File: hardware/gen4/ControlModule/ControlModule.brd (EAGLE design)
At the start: 29.9 x 59.3 mm, 39 parts, among them IC1 XMEGA16A4A

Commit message: changed a resistor value
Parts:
- R8: value 80k -> 80.6k
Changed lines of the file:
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@@
 <?xml version="1.0" encoding="utf-8"?>
 <!DOCTYPE eagle SYSTEM "eagle.dtd">
-<eagle version="7.2.0">
+<eagle version="7.5.0">
 <drawing>
 <settings>
@@
 <attribute name="VALUE" x="41.024" y="8.522" size="0.4064" layer="28" rot="MR180"/>
 </element>
-<element name="R8" library="SparkFun-Passives" package="0805" value="80k" x="44.45" y="20.0025" smashed="yes" rot="MR0">
+<element name="R8" library="SparkFun-Passives" package="0805" value="80.6k" x="44.45" y="20.0025" smashed="yes" rot="MR0">
 <attribute name="NAME" x="45.412" y="21.128" size="0.4064" layer="26" rot="MR0"/>
 <attribute name="VALUE" x="44.166" y="21.2055" size="0.4064" layer="28" rot="MR0"/>

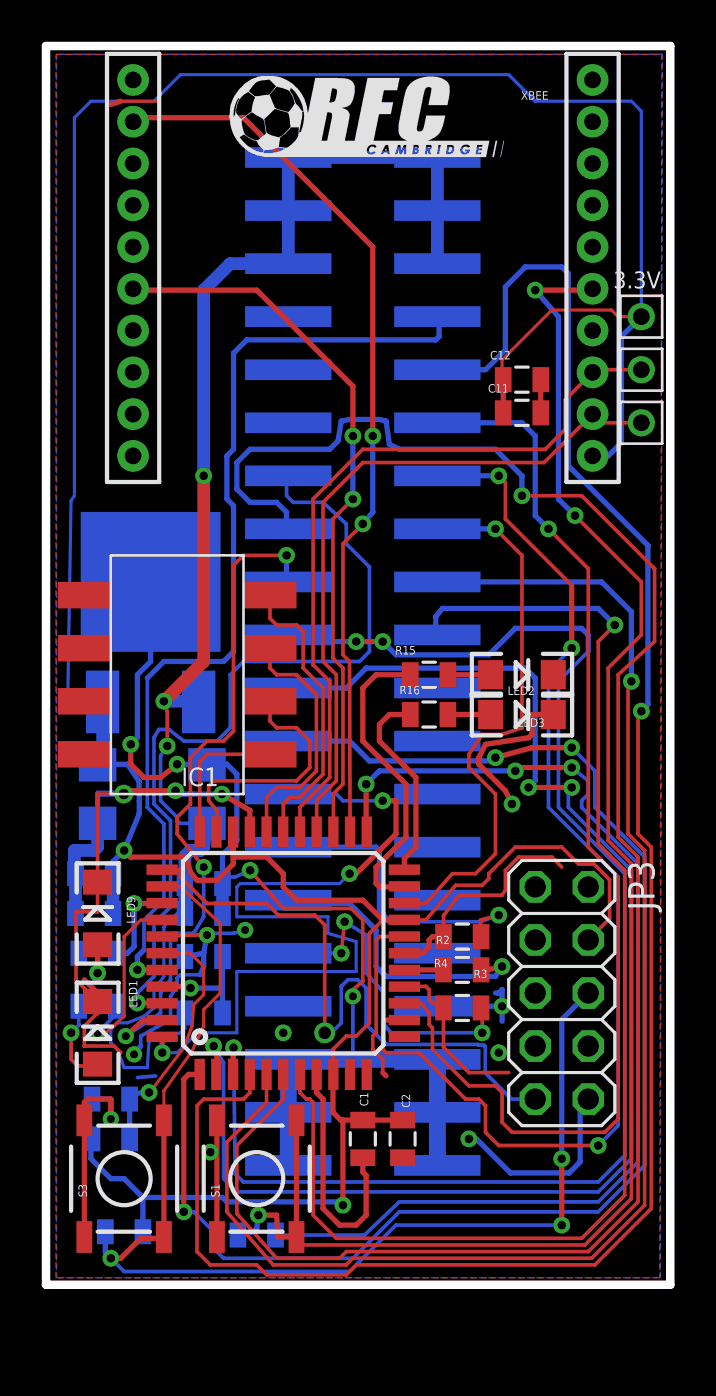
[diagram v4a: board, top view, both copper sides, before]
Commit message: fixed pushbutton on comms board
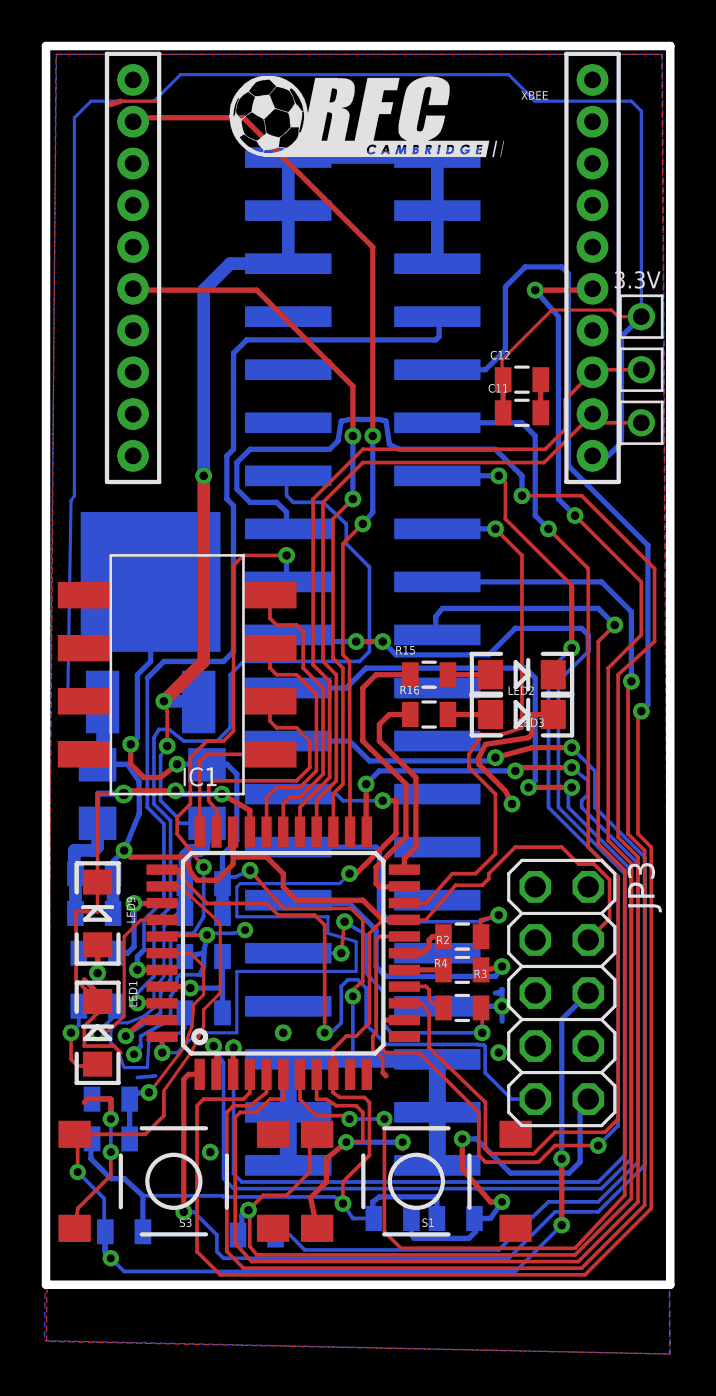
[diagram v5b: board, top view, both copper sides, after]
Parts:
- moved S1 7.65 mm to (54.6, 11.9), turned to 180 degrees
- moved C2 4.58 mm to (56.5, 10.2), flipped to the bottom, turned to 180 degrees
- moved C1 4.07 mm to (53.5, 10.2), flipped to the bottom, turned to 180 degrees
- moved S3 2.38 mm to (43.0, 11.9), turned to 180 degrees
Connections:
- net GND: no longer S1.1, S3.1
- net RESET: no longer S3.3
- net XBRST: no longer S1.3
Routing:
- net SCK: track 11.1 -> 2.39 mm
- net GND: track 117.7 -> 124.8 mm, vias 13 -> 17
- net 3.3V: track 166.8 -> 172.4 mm
- net MISO: track 8.04 -> 2.54 mm
- net RESET: track 58.1 -> 60.7 mm, vias 3 -> 4
- net DISCHARGE: track 90.5 -> 92.4 mm
- net CHARGE_DONE: track 68.4 -> 70.1 mm
- net XBRST: track 76.7 -> 78.1 mm
- net KICK_ENABLE: track 54.1 -> 55.5 mm
- net CHIP_ENABLE: track 54.0 -> 55.1 mm
- net CHARGE: track 61.5 -> 62.1 mm, vias 1 -> 3
- net N$5: track 51.8 -> 52.4 mm

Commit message: comms passes drc this was exhausting
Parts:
- moved R9 0.09 mm to (44.4, 22.6)
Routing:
- net GND: track 124.8 -> 122.2 mm
- net SS_1: track 69.0 -> 71.4 mm
- net 3.3V: track 172.4 -> 171.3 mm
- net BB_OUT: track 91.2 -> 91.9 mm
- net N$7: track 16.3 -> 16.9 mm
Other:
- board size 29.9 x 59.3 mm -> 29.9 x 59.4 mm

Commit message: bit more work
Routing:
- net DISCHARGE: track 92.6 -> 94.7 mm
- net KICK_REF: track 26.7 -> 25.3 mm

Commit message: fixed minor detail about capacitor sizes (using 0.01uF everywhere instead of .01uF on comms)
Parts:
- C11, C6, C7: value .01uF -> 0.01uF
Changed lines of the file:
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@@
 <attribute name="VALUE" x="37.994" y="32.077" size="0.4064" layer="28" rot="MR270"/>
 </element>
-<element name="C11" library="SparkFun-Capacitors" package="0805" value=".01uF" x="59.69" y="48.73625" smashed="yes" rot="R180">
+<element name="C11" library="SparkFun-Capacitors" package="0805" value="0.01uF" x="59.69" y="48.73625" smashed="yes" rot="R180">
 <attribute name="NAME" x="59.052" y="50.11075" size="0.4064" layer="25" rot="R180"/>
 <attribute name="VALUE" x="61.006" y="50.13325" size="0.4064" layer="27" rot="R180"/>
@@
 <element name="C4" library="SparkFun-Capacitors" package="1206" value="47uF" x="44.60875" y="30.48" rot="MR90"/>
 <element name="C5" library="SparkFun-Capacitors" package="0805" value="1uF" x="44.45" y="26.19375" rot="MR180"/>
-<element name="C6" library="SparkFun-Capacitors" package="0805" value=".01uF" x="44.45" y="24.765" rot="MR180"/>
-<element name="C7" library="SparkFun-Capacitors" package="0805" value=".01uF" x="39.21125" y="26.67" smashed="yes" rot="MR0">
+<element name="C6" library="SparkFun-Capacitors" package="0805" value="0.01uF" x="44.45" y="24.765" rot="MR180"/>
+<element name="C7" library="SparkFun-Capacitors" package="0805" value="0.01uF" x="39.21125" y="26.67" smashed="yes" rot="MR0">
 <attribute name="NAME" x="38.67325" y="24.7955" size="0.4064" layer="26" rot="MR0"/>
 <attribute name="VALUE" x="40.62725" y="24.673" size="0.4064" layer="28" rot="MR0"/>
